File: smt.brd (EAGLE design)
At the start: 28.6 x 32.4 mm, 9 parts

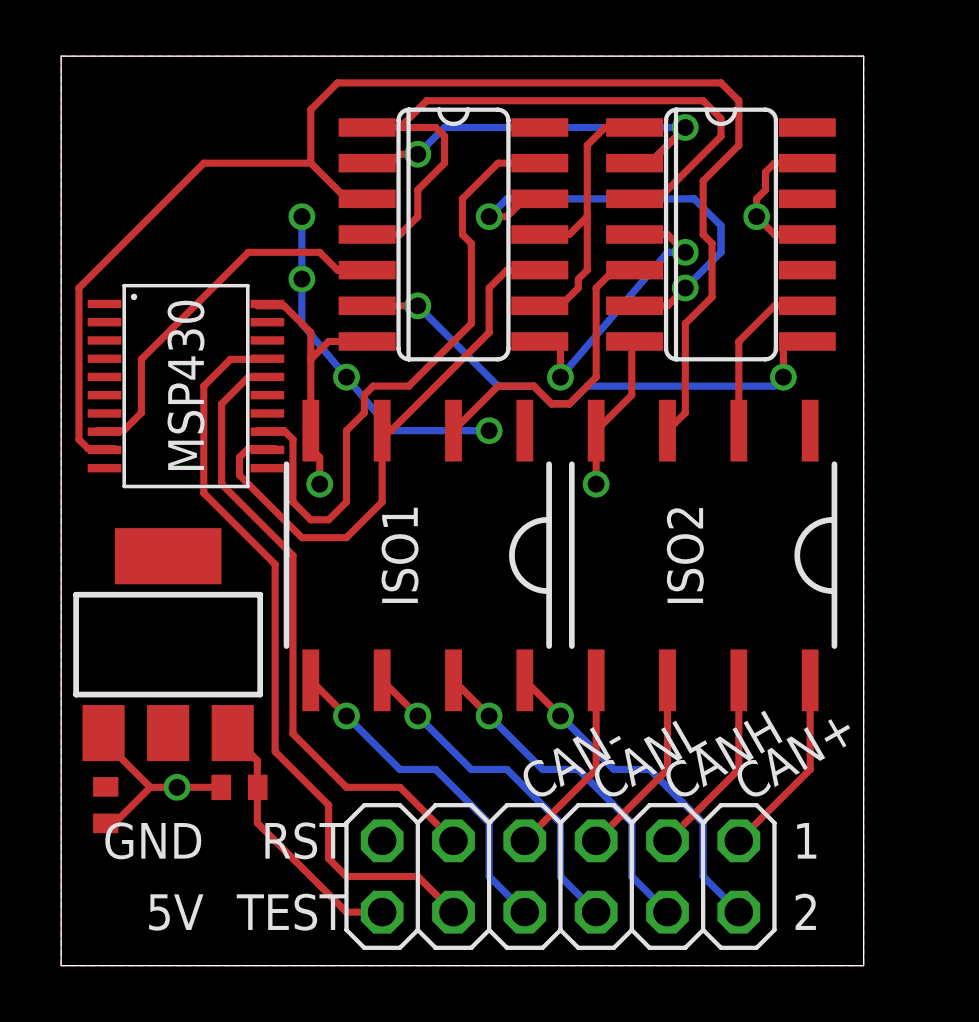
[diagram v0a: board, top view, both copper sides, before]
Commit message: Moved components on thruhole board closer together and swapped pin headers for 1x12 pin header
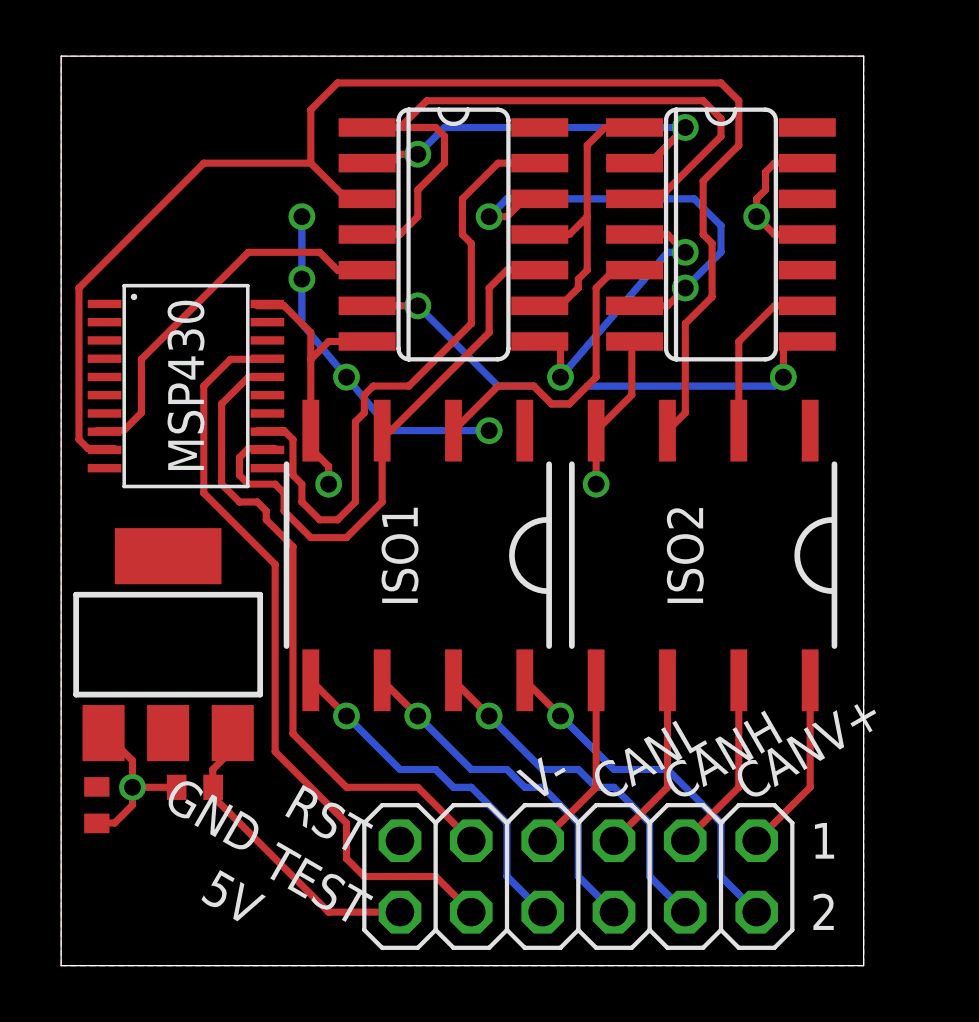
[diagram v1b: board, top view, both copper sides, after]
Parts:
- moved C1 1.59 mm to (4.76, 6.35)
- moved JP1 0.63 mm to (18.4, 3.17)
- moved C2 0.32 mm to (1.27, 5.71)
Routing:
- net N$23: track 9.33 -> 10.9 mm
- net N$1: track 22.4 -> 23.4 mm
- net GND: track 30.3 -> 29.6 mm
- net N$13: track 12.2 -> 12.8 mm
- net N$14: track 12.2 -> 12.8 mm
- net N$16: track 12.2 -> 12.8 mm
- net N$15: track 12.2 -> 12.8 mm
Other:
- board text added: "CANV+"
- board text added: "V-"
- board text removed: "CAN+"
- board text removed: "CAN-"

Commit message: Adjusted SMT board pin labels
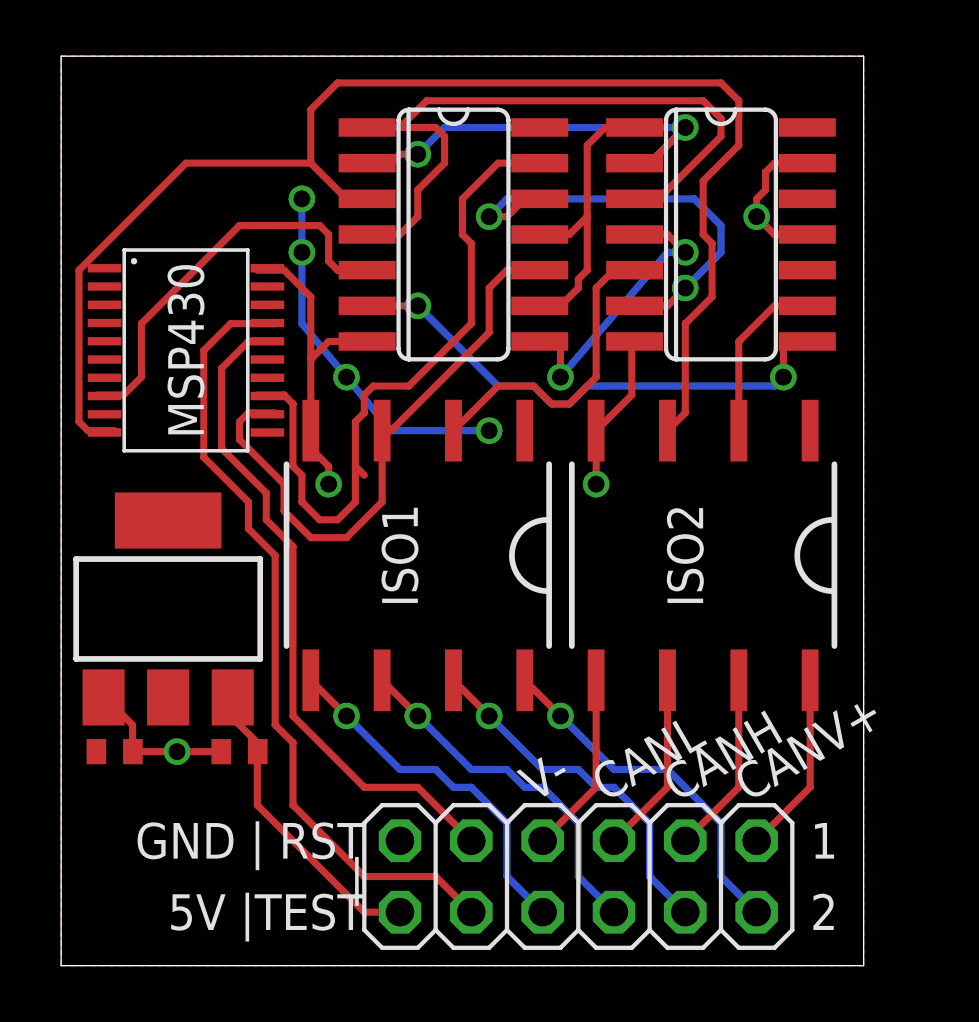
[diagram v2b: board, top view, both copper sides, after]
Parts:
- moved C1 2.03 mm to (6.35, 7.62)
- moved C2 2.01 mm to (1.91, 7.62), turned to 0 degrees
- moved LD117AV33 1.27 mm to (3.81, 12.7)
- moved MSP430 1.27 mm to (4.45, 21.9)
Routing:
- net N$22: track 23.0 -> 24.7 mm
- net N$2: track 27.1 -> 28.4 mm
- net N$21: track 13.5 -> 14.4 mm
- net N$25: track 20.5 -> 21.2 mm
- net GND: track 29.6 -> 30.3 mm
- net VCC: track 12.3 -> 12.9 mm
- net N$1: track 23.4 -> 23.9 mm
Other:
- board text added: "5V |TEST"
- board text added: "GND | RST"
- board text added: "|"
- board text removed: "5V"
- board text removed: "GND"
- board text removed: "RST"
- board text removed: "TEST"

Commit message: Removed errant trace from SMT board
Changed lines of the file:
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@@
 <wire x1="12.3825" y1="20.6375" x2="11.1125" y2="20.6375" width="0.254" layer="1"/>
 <wire x1="11.1125" y1="20.6375" x2="10.795" y2="20.32" width="0.254" layer="1"/>
-<wire x1="10.4775" y1="19.3675" x2="10.4775" y2="17.78" width="0.254" layer="1"/>
-<wire x1="10.4775" y1="17.78" x2="10.4775" y2="16.51" width="0.254" layer="1"/>
+<wire x1="10.4775" y1="19.3675" x2="10.4775" y2="16.51" width="0.254" layer="1"/>
+<wire x1="10.4775" y1="17.78" x2="10.4775" y2="16.51" width="0" layer="19" extent="1-16"/>
 <wire x1="10.4775" y1="16.51" x2="9.8425" y2="15.875" width="0.254" layer="1"/>
 <wire x1="9.8425" y1="15.875" x2="9.2075" y2="15.875" width="0.254" layer="1"/>
@@
 <wire x1="8.5725" y1="17.4625" x2="8.5725" y2="16.51" width="0.254" layer="1"/>
 <wire x1="8.5725" y1="16.51" x2="9.2075" y2="15.875" width="0.254" layer="1"/>
-<wire x1="10.4775" y1="17.78" x2="10.795" y2="17.4625" width="0.254" layer="1"/>
+<wire x1="10.4775" y1="17.78" x2="10.795" y2="17.4625" width="0" layer="19" extent="1-16"/>
 <wire x1="17.145" y1="28.575" x2="17.0434" y2="28.575" width="0" layer="19" extent="1-1"/>
 <wire x1="7.345" y1="20.2825" x2="6.985" y2="20.32" width="0" layer="19" extent="1-1"/>
